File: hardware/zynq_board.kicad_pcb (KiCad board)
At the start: 8 copper layers, 120 x 75 mm, 412 parts, among them J1 USB_OTG, J10 DM3CS, J11 USB_OTG, J12 Conn_01x02, J6 MDR20, J7 LSHM-150-xxx-x-DV-A-S, J9 Conn_01x02, Q1 DMP3056L, U1 xc7z030sbg485, U10 TPS3808G01, U11 MCP1700-2502E_SOT23, U12 MT41K128M8, U13 TPS51206, U14 MT41K128M8, U15 DIFF_OSC, U16 DIFF_OSC, U17 SI53340, U18 NX5P3090, U19 SMP1255PUTG, U2 SFPP_CONN, U20 USB3320, U21 OSC, U22 TLK10031, U23 SN74AXC8T245, U24 SN74AXC8T245, U25 SN74AXC8T245, U26 LSF0102, U27 LSF0102, U28 SN74LVC2T45, U29 SN74LVC2T45, U3 TPS8208x, U30 SN74LVC2T45, U31 SN74LVC2T45, U32 DMF05LCFLP, U33 DMF05LCFLP, U34 TC1262-33, U35 MAX14854, U36 CAT24C02TDI-GT3, U37 EMIF06-MSD02N16, U38 33.333MHZ, U39 SMP1255PUTG, U4 TPS8208x, U40 FT234XD, U41 SN74LV1T126, U42 SN74LV1T126, U5 TPSM84424, U6 TPSM84424, U7 TPS8208x, U8 TPS8208x, U9 TPS8208x

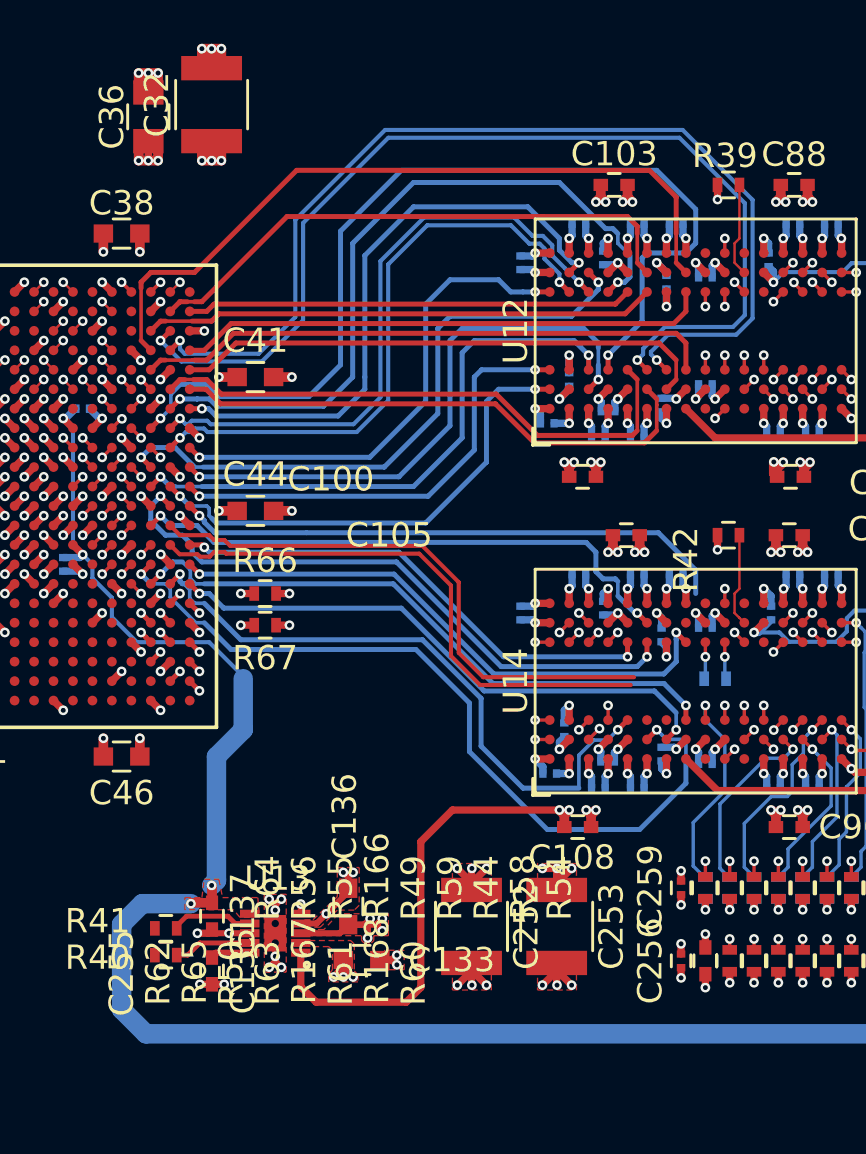
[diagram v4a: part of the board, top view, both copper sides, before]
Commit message: Length matched DDR3 Traces.
TODO: evtl. GND Stiching, DDR3 Power, diff. Lane Skew correction.
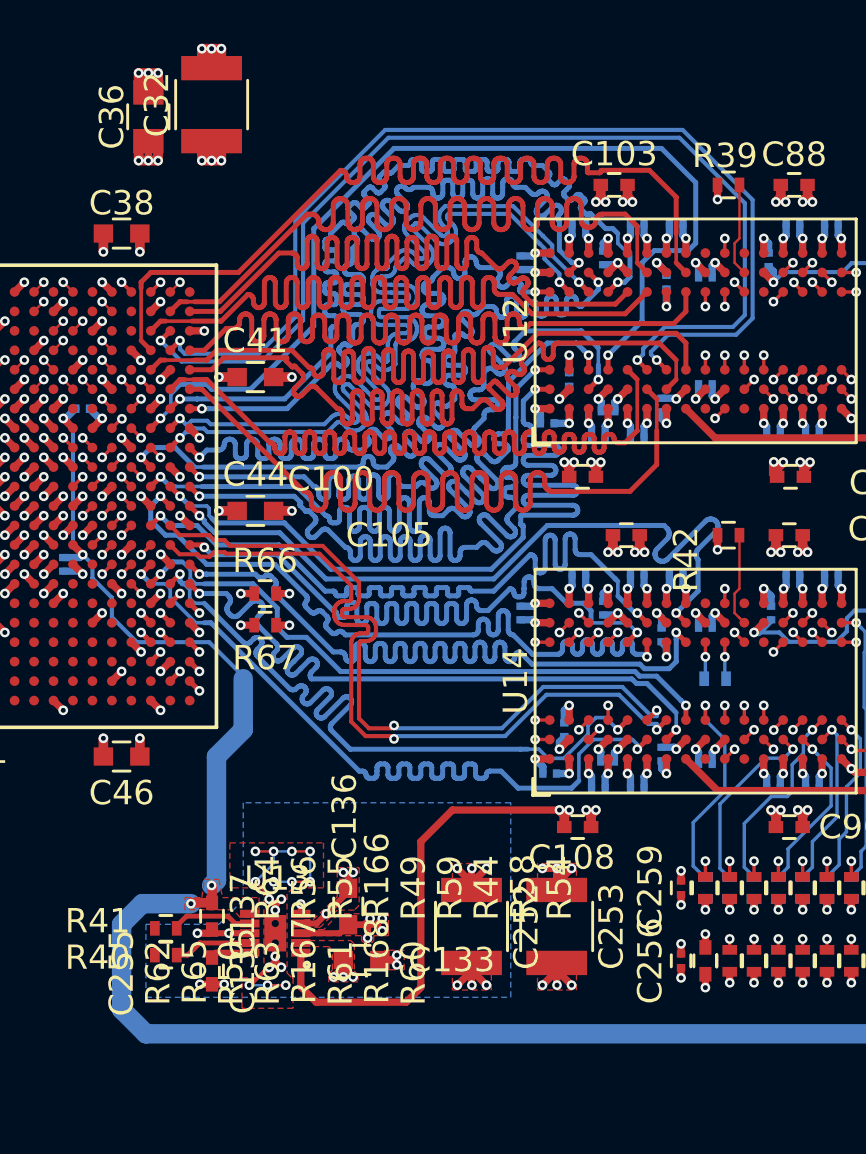
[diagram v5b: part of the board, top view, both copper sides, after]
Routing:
- net /DDR/DDR_DM0: track 18.3 -> 42.1 mm
- net /DDR/DQ1: track 21.1 -> 44.6 mm
- net /DDR/DQ6: track 23.1 -> 46.5 mm
- net /DDR/DQ7: track 22.2 -> 45.1 mm
- net /DDR/DQ5: track 22.1 -> 43.9 mm
- net /DDR/DQ0: track 21.9 -> 43.3 mm
- net /DDR/DQ4: track 24.0 -> 44.9 mm
- net /DDR/DQ2: track 23.0 -> 42.2 mm
- net /DDR/DQ10: track 18.9 -> 37.7 mm
- net /DDR/DQ14: track 20.5 -> 38.9 mm
- net /DDR/DQ12: track 23.7 -> 41.7 mm
- net /DDR/DQ11: track 20.1 -> 37.4 mm
- net /DDR/DQ13: track 23.9 -> 40.6 mm
- net /DDR/DQ9: track 24.7 -> 40.7 mm
- net /DDR/DQ3: track 30.6 -> 44.7 mm
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- added copper zone on B.Cu, net GND
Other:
- board text added: "TODO: Correct Skew/Phase at DDR3 Memorys differential Lanes"
- board text added: "TODO: Maybe add GND Stiching Vias"
- board text removed: "TODO: Connect DQS3"

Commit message: Moved the bigger ICs and Connectors to the board to think about placing the connectors.
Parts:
- removed the REF** at (140.7, 72.1)
- removed the REF** at (109.7, 72.1)
- added REF**: MountingHole_3.2mm_M3, Mounting_Holes:MountingHole_3.2mm_M3, F.Cu at (160.0, 64.0)
- J10: moved to B.Cu
- moved U42 259.7 mm to (138.6, 79.2), turned to 90 degrees
- moved U36 254.5 mm to (126.5, 93.9), turned to 90 degrees
- moved U39 249.1 mm to (128.2, 68.1)
- moved U23 245.3 mm to (123.8, 88.2), turned to 0 degrees
- moved J11 239.1 mm to (127.8, 64.3)
- moved U40 237.9 mm to (136.8, 74.6)
- moved U41 235.6 mm to (125.8, 76.8), turned to 270 degrees
- moved U25 229.7 mm to (109.6, 88.2)
- moved U24 227.0 mm to (116.7, 88.1), turned to 0 degrees
- moved U18 196.5 mm to (120.6, 69.2)
- moved U11 194.3 mm to (122.0, 81.2)
- moved U19 194.2 mm to (117.5, 68.5)
- moved U10 176.6 mm to (99.8, 85.8), turned to 180 degrees
- moved U28 172.2 mm to (100.0, 95.5)
- moved U9 172.0 mm to (104.3, 80.8)
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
